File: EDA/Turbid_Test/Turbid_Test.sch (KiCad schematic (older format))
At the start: 4 parts

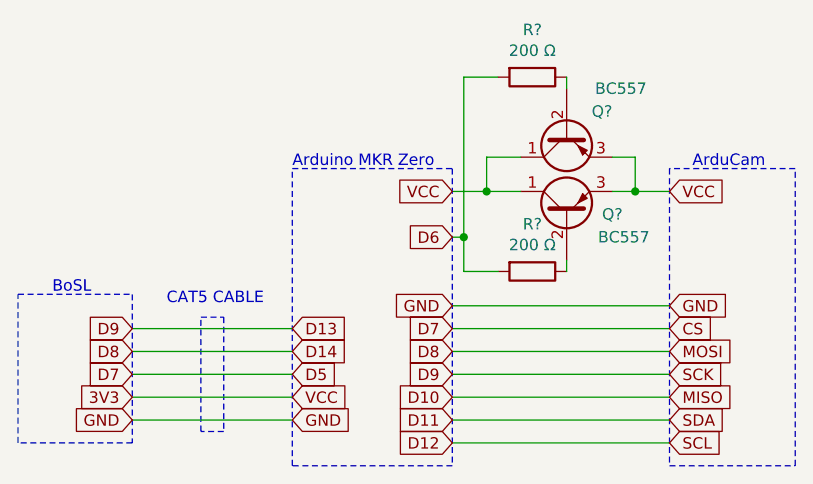
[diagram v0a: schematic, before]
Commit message: added shorter case
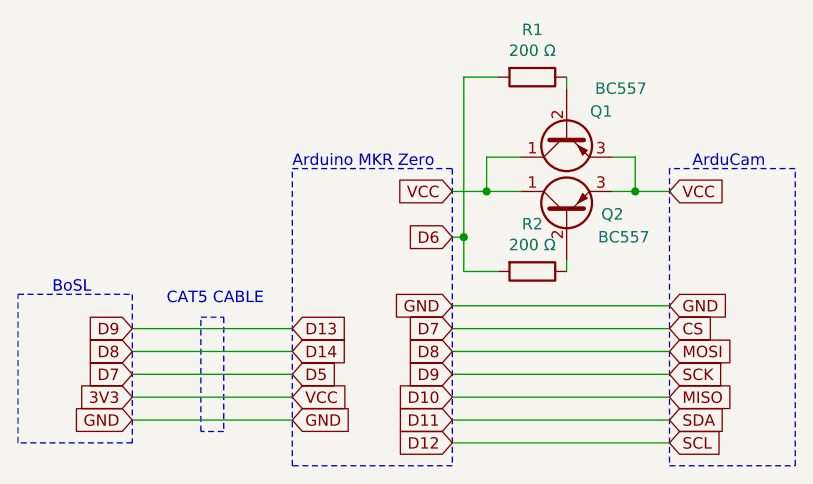
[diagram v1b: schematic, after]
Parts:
- gave numbers to parts that had none: 4
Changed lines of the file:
@@
 VCC
 $Comp
-L Transistor_BJT:BC557 Q?
+L Transistor_BJT:BC557 Q2
 U 1 1 5F1688A6
 P 4450 1600
-F 0 "Q?" V 4450 1400 50  0000 C CNN
+F 0 "Q2" V 4450 1400 50  0000 C CNN
 F 1 "BC557" V 4350 1350 50  0000 C CNN
 F 2 "Package_TO_SOT_THT:TO-92_Inline" H 4650 1525 50  0001 L CIN
@@
 $EndComp
 $Comp
-L Transistor_BJT:BC557 Q?
+L Transistor_BJT:BC557 Q1
 U 1 1 5F16910C
 P 4450 1250
-F 0 "Q?" V 4350 1050 50  0000 L CNN
+F 0 "Q1" V 4350 1050 50  0000 L CNN
 F 1 "BC557" V 4250 900 50  0000 L CNN
 F 2 "Package_TO_SOT_THT:TO-92_Inline" H 4650 1175 50  0001 L CIN
@@
 Connection ~ 4100 1500
 $Comp
-L Device:R R?
+L Device:R R2
 U 1 1 5F173B21
 P 4300 1850
-F 0 "R?" V 4093 1850 50  0000 C CNN
+F 0 "R2" V 4093 1850 50  0000 C CNN
 F 1 "200 Ω" V 4184 1850 50  0000 C CNN
 F 2 "" V 4230 1850 50  0001 C CNN
@@
 $EndComp
 $Comp
-L Device:R R?
+L Device:R R1
 U 1 1 5F1741D2
 P 4300 1000
-F 0 "R?" V 4093 1000 50  0000 C CNN
+F 0 "R1" V 4093 1000 50  0000 C CNN
 F 1 "200 Ω" V 4184 1000 50  0000 C CNN
 F 2 "" V 4230 1000 50  0001 C CNN
